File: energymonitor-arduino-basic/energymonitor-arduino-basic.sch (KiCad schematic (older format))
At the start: 12 parts

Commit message: Add conector for 1 wire temperature
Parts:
- added C?: C, symbol Device:C
- added J?: Conn_01x03_Female, symbol Connector:Conn_01x03_Female
- added R?: 4k7, Resistor_THT:R_Axial_DIN0207_L6.3mm_D2.5mm_P10.16mm_Horizontal, symbol Device:R
- J?: value Conn_01x04_Female -> Conn_01x05_Female; symbol Connector:Conn_01x04_Female -> Connector:Conn_01x05_Female
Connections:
- net labels added: 1wire-bus
- wire segments 44 -> 58
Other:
- note added: "9v AC"
- note added: "CT Sensor"
- note added: "DS18B20"
- note added: "Data"
- note added: "Data pull-up resistor"
- note added: "GND"
- note added: "VCC"
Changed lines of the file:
@@
 $EndDescr
 $Comp
-L Connector:Conn_01x04_Female J?
+L Connector:Conn_01x05_Female J?
 U 1 1 62606ACB
-P 7150 1400
-F 0 "J?" H 7178 1376 50  0000 L CNN
-F 1 "Conn_01x04_Female" H 7178 1285 50  0000 L CNN
-F 2 "" H 7150 1400 50  0001 C CNN
-F 3 "~" H 7150 1400 50  0001 C CNN
-	1    7150 1400
-	1    0    0    -1
-$EndComp
-$Comp
-L power:+5V #PWR?
+P 7150 1500
+F 0 "J?" H 7178 1476 50  0000 L CNN
+F 1 "Conn_01x05_Female" H 7178 1385 50  0000 L CNN
+F 2 "" H 7150 1500 50  0001 C CNN
+F 3 "~" H 7150 1500 50  0001 C CNN
+	1    7150 1500
+	1    0    0    -1
+$EndComp
+$Comp
+L power:+5V #PWR0101
 U 1 1 626076B4
 P 6150 1050
-F 0 "#PWR?" H 6150 900 50  0001 C CNN
+F 0 "#PWR0101" H 6150 900 50  0001 C CNN
 F 1 "+5V" H 6165 1223 50  0000 C CNN
 F 2 "" H 6150 1050 50  0001 C CNN
@@
 $EndComp
 $Comp
-L power:GND #PWR?
+L power:GND #PWR0102
 U 1 1 62607C1A
 P 6150 2550
-F 0 "#PWR?" H 6150 2300 50  0001 C CNN
+F 0 "#PWR0102" H 6150 2300 50  0001 C CNN
 F 1 "GND" H 6155 2377 50  0000 C CNN
 F 2 "" H 6150 2550 50  0001 C CNN
@@
 $EndComp
 $Comp
-L power:GND #PWR?
+L power:GND #PWR0103
 U 1 1 6260B66F
 P 2250 2150
-F 0 "#PWR?" H 2250 1900 50  0001 C CNN
+F 0 "#PWR0103" H 2250 1900 50  0001 C CNN
 F 1 "GND" H 2255 1977 50  0000 C CNN
 F 2 "" H 2250 2150 50  0001 C CNN
@@
 NoConn ~ 2450 1500
 $Comp
-L power:GND #PWR?
+L power:GND #PWR0104
 U 1 1 62619158
 P 3350 2800
-F 0 "#PWR?" H 3350 2550 50  0001 C CNN
+F 0 "#PWR0104" H 3350 2550 50  0001 C CNN
 F 1 "GND" H 3355 2627 50  0000 C CNN
 F 2 "" H 3350 2800 50  0001 C CNN
@@
 $EndComp
 $Comp
-L power:+5V #PWR?
+L power:+5V #PWR0105
 U 1 1 62619507
 P 3900 2200
-F 0 "#PWR?" H 3900 2050 50  0001 C CNN
+F 0 "#PWR0105" H 3900 2050 50  0001 C CNN
 F 1 "+5V" V 3915 2328 50  0000 L CNN
 F 2 "" H 3900 2200 50  0001 C CNN
@@
 $EndComp
 $Comp
-L power:+5V #PWR?
+L power:+5V #PWR0106
 U 1 1 6262D570
 P 3900 4300
-F 0 "#PWR?" H 3900 4150 50  0001 C CNN
+F 0 "#PWR0106" H 3900 4150 50  0001 C CNN
 F 1 "+5V" V 3915 4428 50  0000 L CNN
 F 2 "" H 3900 4300 50  0001 C CNN
@@
 $EndComp
 $Comp
-L power:GND #PWR?
+L power:GND #PWR0107
 U 1 1 6262E712
 P 3350 5000
-F 0 "#PWR?" H 3350 4750 50  0001 C CNN
+F 0 "#PWR0107" H 3350 4750 50  0001 C CNN
 F 1 "GND" H 3355 4827 50  0000 C CNN
 F 2 "" H 3350 5000 50  0001 C CNN
@@
 Text Notes 2400 3800 0    50   ~ 0
 Step down voltage divider
+Text Label 6750 1700 2    50   ~ 0
+1wire-bus
+Wire Wire Line
+	6950 1700 6750 1700
+$Comp
+L Connector:Conn_01x03_Female J?
+U 1 1 6261A3BF
+P 5550 3550
+F 0 "J?" H 5442 3225 50  0000 C CNN
+F 1 "Conn_01x03_Female" H 5442 3316 50  0000 C CNN
+F 2 "" H 5550 3550 50  0001 C CNN
+F 3 "~" H 5550 3550 50  0001 C CNN
+	1    5550 3550
+	-1   0    0    1
+$EndComp
+$Comp
+L power:GND #PWR0108
+U 1 1 6261B219
+P 6000 3200
+F 0 "#PWR0108" H 6000 2950 50  0001 C CNN
+F 1 "GND" H 6005 3027 50  0000 C CNN
+F 2 "" H 6000 3200 50  0001 C CNN
+F 3 "" H 6000 3200 50  0001 C CNN
+	1    6000 3200
+	-1   0    0    1
+$EndComp
+$Comp
+L power:+5V #PWR0109
+U 1 1 6261B786
+P 6550 3200
+F 0 "#PWR0109" H 6550 3050 50  0001 C CNN
+F 1 "+5V" H 6565 3373 50  0000 C CNN
+F 2 "" H 6550 3200 50  0001 C CNN
+F 3 "" H 6550 3200 50  0001 C CNN
+	1    6550 3200
+	1    0    0    -1
+$EndComp
+Text Label 7150 3650 0    50   ~ 0
+1wire-bus
+$Comp
+L Device:R R?
+U 1 1 6261CDC5
+P 6800 3550
+F 0 "R?" V 6593 3550 50  0000 C CNN
+F 1 "4k7" V 6684 3550 50  0000 C CNN
+F 2 "Resistor_THT:R_Axial_DIN0207_L6.3mm_D2.5mm_P10.16mm_Horizontal" V 6730 3550 50  0001 C CNN
+F 3 "~" H 6800 3550 50  0001 C CNN
+	1    6800 3550
+	0    1    1    0
+$EndComp
+Wire Wire Line
+	6950 3550 7050 3550
+Wire Wire Line
+	7050 3550 7050 3650
+Connection ~ 7050 3650
+Wire Wire Line
+	7050 3650 7150 3650
+Wire Wire Line
+	6650 3550 6550 3550
+Wire Wire Line
+	6550 3200 6550 3350
+Connection ~ 6550 3550
+Wire Wire Line
+	6000 3200 6000 3350
+Wire Wire Line
+	6000 3450 5750 3450
+Text Notes 7000 3450 0    50   ~ 0
+Data pull-up resistor
+Wire Wire Line
+	5750 3550 6550 3550
+Wire Wire Line
+	5750 3650 7050 3650
+Wire Wire Line
+	6150 3350 6000 3350
+Connection ~ 6000 3350
+Wire Wire Line
+	6000 3350 6000 3450
+Wire Wire Line
+	6450 3350 6550 3350
+Connection ~ 6550 3350
+Wire Wire Line
+	6550 3350 6550 3550
+$Comp
+L Device:C C?
+U 1 1 6263CCEC
+P 6300 3350
+F 0 "C?" V 6048 3350 50  0000 C CNN
+F 1 "C" V 6139 3350 50  0000 C CNN
+F 2 "" H 6338 3200 50  0001 C CNN
+F 3 "~" H 6300 3350 50  0001 C CNN
+	1    6300 3350
+	0    1    1    0
+$EndComp
+Text Notes 5350 3650 0    50   ~ 0
+Data
+Text Notes 5350 3550 0    50   ~ 0
+VCC
+Text Notes 5350 3450 0    50   ~ 0
+GND
+Text Notes 1650 1900 0    50   ~ 0
+CT Sensor
+Text Notes 1750 3850 0    50   ~ 0
+9v AC
+Text Notes 5050 3800 0    50   ~ 0
+DS18B20
 $EndSCHEMATC

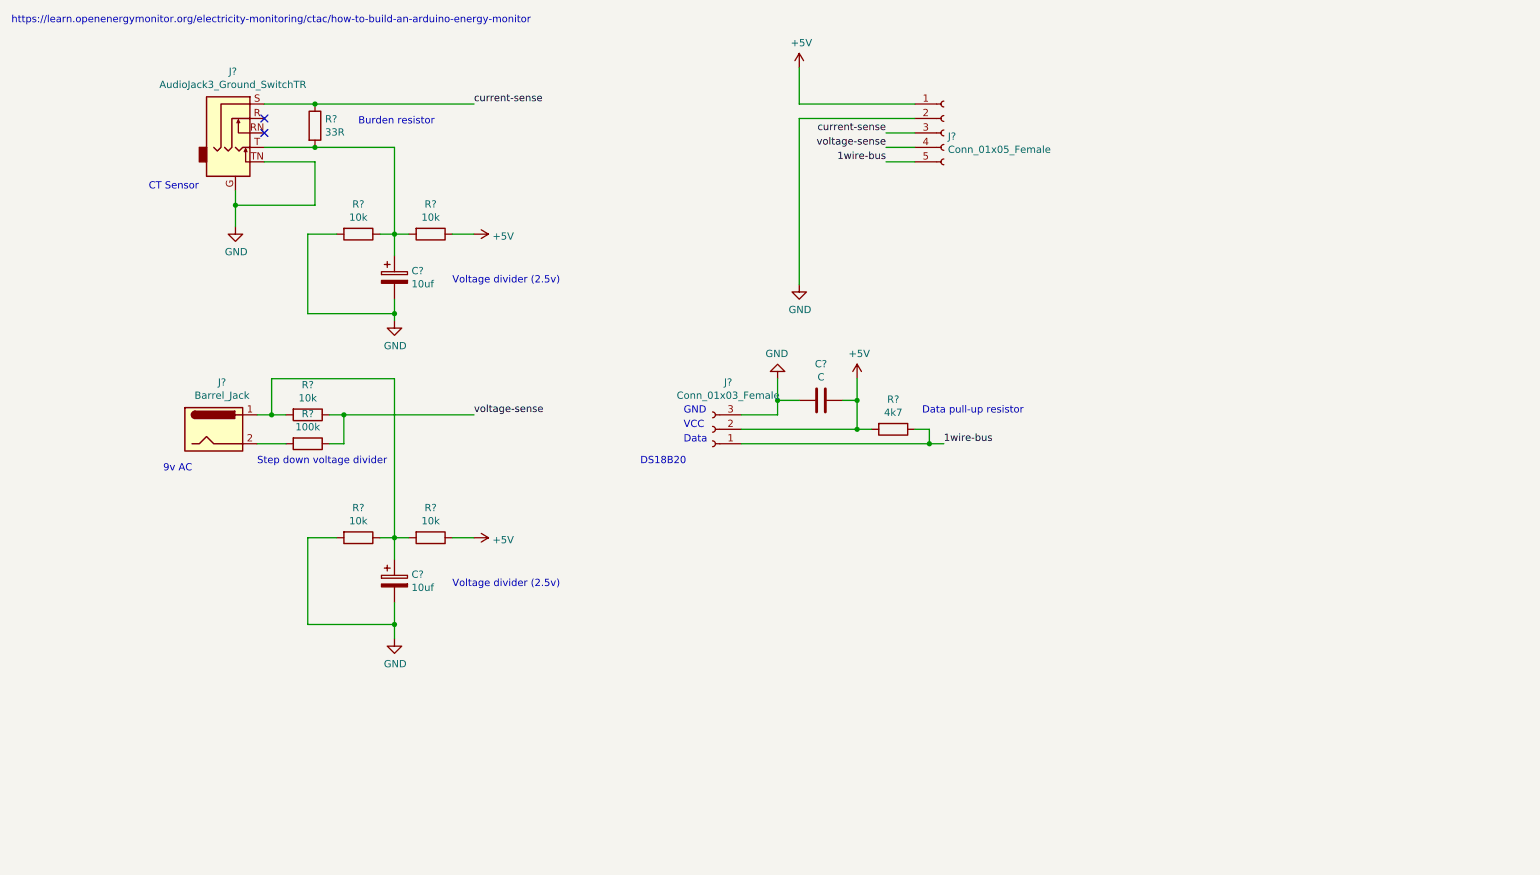
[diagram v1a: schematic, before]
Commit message: Use buffered midpoint voltage
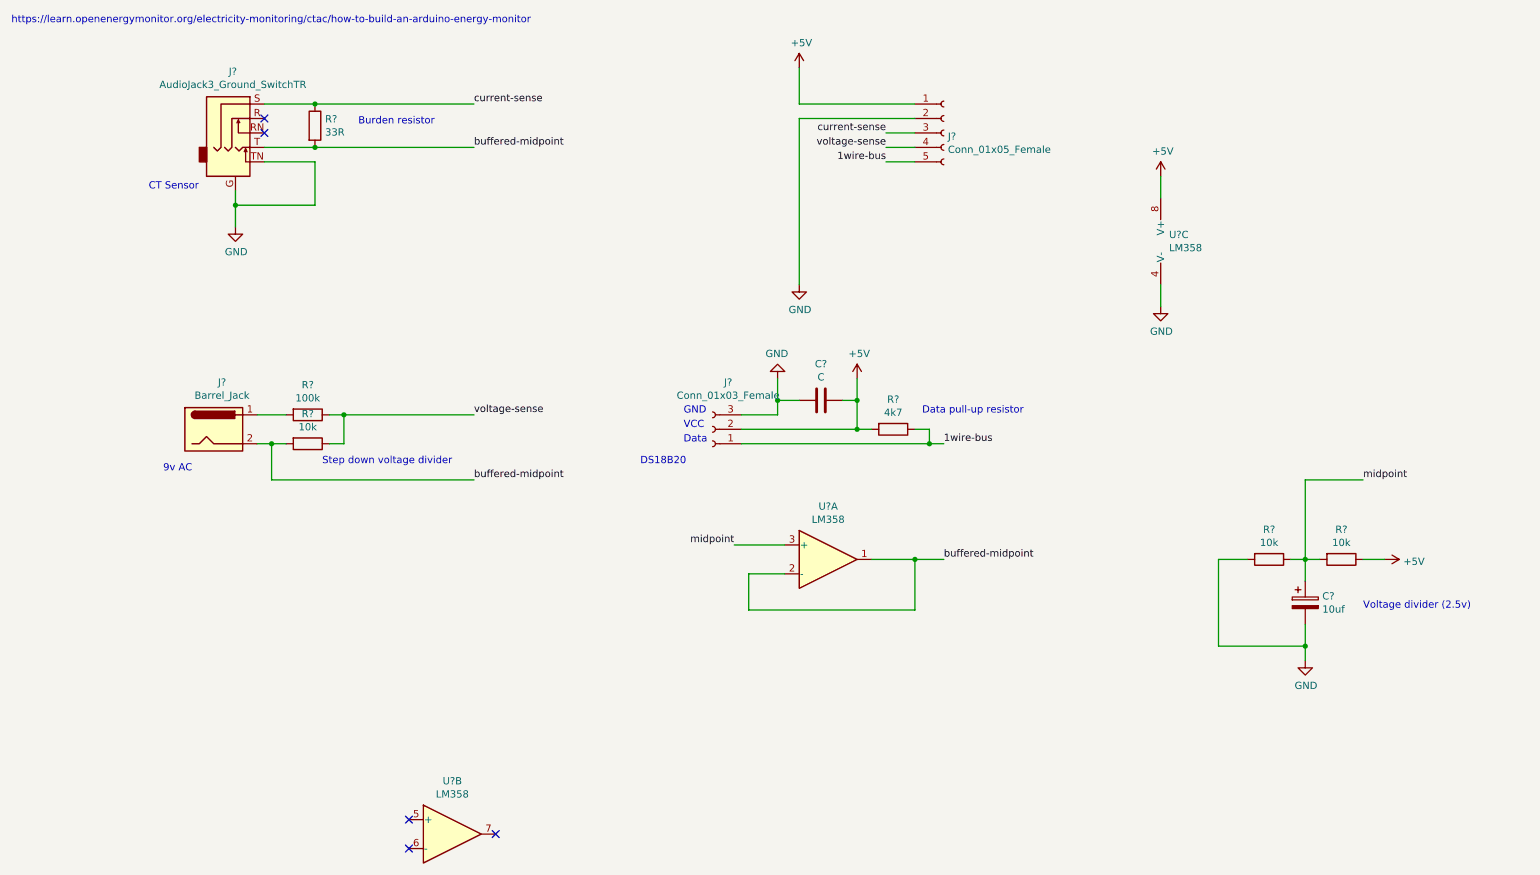
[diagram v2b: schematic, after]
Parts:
- removed C?: 10uf, symbol Device:CP
- removed R? (x2): 10k, Resistor_THT:R_Axial_DIN0207_L6.3mm_D2.5mm_P10.16mm_Horizontal, symbol Device:R
- added U? (x3): LM358, symbol Amplifier_Operational:LM358
- R?: value 10k -> 100k
- R?: value 100k -> 10k
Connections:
- net +5V: now also U?.8 (V+)
- net GND: now also U?.4 (V-)
- net buffered-midpoint: now reaches J?.T, R?.2
- net buffered-midpoint: now also J?.2, R?.2, U?.1, U?.2 (-)
- net midpoint: now reaches C?.1, R?.1, R?.2
- net midpoint: now also U?.3 (+); no longer J?.1, R?.2
- new net: J?.1, R?.2
- no-connect marks 2 -> 5
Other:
- moved on the sheet: C?, R?
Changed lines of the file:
@@
 	2250 2150 2250 2000
-$Comp
-L Device:CP C?
-U 1 1 6260BDA8
-P 3350 2500
-F 0 "C?" H 3468 2546 50  0000 L CNN
-F 1 "10uf" H 3468 2455 50  0000 L CNN
-F 2 "" H 3388 2350 50  0001 C CNN
-F 3 "~" H 3350 2500 50  0001 C CNN
-	1    3350 2500
-	1    0    0    -1
-$EndComp
-$Comp
-L Device:R R?
-U 1 1 6260C4FE
-P 3100 2200
-F 0 "R?" V 2893 2200 50  0000 C CNN
-F 1 "10k" V 2984 2200 50  0000 C CNN
-F 2 "Resistor_THT:R_Axial_DIN0207_L6.3mm_D2.5mm_P10.16mm_Horizontal" V 3030 2200 50  0001 C CNN
-F 3 "~" H 3100 2200 50  0001 C CNN
-	1    3100 2200
-	0    1    1    0
-$EndComp
-$Comp
-L Device:R R?
-U 1 1 6260C5C9
-P 3600 2200
-F 0 "R?" V 3393 2200 50  0000 C CNN
-F 1 "10k" V 3484 2200 50  0000 C CNN
-F 2 "Resistor_THT:R_Axial_DIN0207_L6.3mm_D2.5mm_P10.16mm_Horizontal" V 3530 2200 50  0001 C CNN
-F 3 "~" H 3600 2200 50  0001 C CNN
-	1    3600 2200
-	0    1    1    0
-$EndComp
 $Comp
 L Device:R R?
@@
 NoConn ~ 2450 1400
 NoConn ~ 2450 1500
-$Comp
-L power:GND #PWR0104
-U 1 1 62619158
-P 3350 2800
-F 0 "#PWR0104" H 3350 2550 50  0001 C CNN
-F 1 "GND" H 3355 2627 50  0000 C CNN
-F 2 "" H 3350 2800 50  0001 C CNN
-F 3 "" H 3350 2800 50  0001 C CNN
-	1    3350 2800
-	1    0    0    -1
-$EndComp
-$Comp
-L power:+5V #PWR0105
-U 1 1 62619507
-P 3900 2200
-F 0 "#PWR0105" H 3900 2050 50  0001 C CNN
-F 1 "+5V" V 3915 2328 50  0000 L CNN
-F 2 "" H 3900 2200 50  0001 C CNN
-F 3 "" H 3900 2200 50  0001 C CNN
-	1    3900 2200
-	0    1    1    0
-$EndComp
-Wire Wire Line
-	3250 2200 3350 2200
-Wire Wire Line
-	3350 2350 3350 2200
-Connection ~ 3350 2200
-Wire Wire Line
-	3350 2200 3450 2200
-Wire Wire Line
-	3900 2200 3750 2200
-Wire Wire Line
-	2950 2200 2750 2200
-Wire Wire Line
-	2750 2200 2750 2750
-Wire Wire Line
-	2750 2750 3350 2750
-Wire Wire Line
-	3350 2750 3350 2650
-Wire Wire Line
-	3350 2800 3350 2750
-Connection ~ 3350 2750
-Wire Wire Line
-	3350 2200 3350 1600
-Wire Wire Line
-	3350 1600 2800 1600
 Connection ~ 2800 1600
 Text Label 3900 1300 0    50   ~ 0
@@
 L Device:R R?
 U 1 1 6262BC5E
-P 3100 4300
-F 0 "R?" V 2893 4300 50  0000 C CNN
-F 1 "10k" V 2984 4300 50  0000 C CNN
-F 2 "Resistor_THT:R_Axial_DIN0207_L6.3mm_D2.5mm_P10.16mm_Horizontal" V 3030 4300 50  0001 C CNN
-F 3 "~" H 3100 4300 50  0001 C CNN
-	1    3100 4300
+P 9400 4450
+F 0 "R?" V 9193 4450 50  0000 C CNN
+F 1 "10k" V 9284 4450 50  0000 C CNN
+F 2 "Resistor_THT:R_Axial_DIN0207_L6.3mm_D2.5mm_P10.16mm_Horizontal" V 9330 4450 50  0001 C CNN
+F 3 "~" H 9400 4450 50  0001 C CNN
+	1    9400 4450
 	0    1    1    0
 $EndComp
@@
 L Device:R R?
 U 1 1 6262C6E4
-P 3600 4300
-F 0 "R?" V 3393 4300 50  0000 C CNN
-F 1 "10k" V 3484 4300 50  0000 C CNN
-F 2 "Resistor_THT:R_Axial_DIN0207_L6.3mm_D2.5mm_P10.16mm_Horizontal" V 3530 4300 50  0001 C CNN
-F 3 "~" H 3600 4300 50  0001 C CNN
-	1    3600 4300
+P 9900 4450
+F 0 "R?" V 9693 4450 50  0000 C CNN
+F 1 "10k" V 9784 4450 50  0000 C CNN
+F 2 "Resistor_THT:R_Axial_DIN0207_L6.3mm_D2.5mm_P10.16mm_Horizontal" V 9830 4450 50  0001 C CNN
+F 3 "~" H 9900 4450 50  0001 C CNN
+	1    9900 4450
 	0    1    1    0
 $EndComp
@@
 L Device:CP C?
 U 1 1 6262CCE6
-P 3350 4600
-F 0 "C?" H 3468 4646 50  0000 L CNN
-F 1 "10uf" H 3468 4555 50  0000 L CNN
-F 2 "" H 3388 4450 50  0001 C CNN
-F 3 "~" H 3350 4600 50  0001 C CNN
-	1    3350 4600
+P 9650 4750
+F 0 "C?" H 9768 4796 50  0000 L CNN
+F 1 "10uf" H 9768 4705 50  0000 L CNN
+F 2 "" H 9688 4600 50  0001 C CNN
+F 3 "~" H 9650 4750 50  0001 C CNN
+	1    9650 4750
 	1    0    0    -1
 $EndComp
@@
 L power:+5V #PWR0106
 U 1 1 6262D570
-P 3900 4300
-F 0 "#PWR0106" H 3900 4150 50  0001 C CNN
-F 1 "+5V" V 3915 4428 50  0000 L CNN
-F 2 "" H 3900 4300 50  0001 C CNN
-F 3 "" H 3900 4300 50  0001 C CNN
-	1    3900 4300
+P 10200 4450
+F 0 "#PWR0106" H 10200 4300 50  0001 C CNN
+F 1 "+5V" V 10215 4578 50  0000 L CNN
+F 2 "" H 10200 4450 50  0001 C CNN
+F 3 "" H 10200 4450 50  0001 C CNN
+	1    10200 4450
 	0    1    1    0
 $EndComp
@@
 L power:GND #PWR0107
 U 1 1 6262E712
-P 3350 5000
-F 0 "#PWR0107" H 3350 4750 50  0001 C CNN
-F 1 "GND" H 3355 4827 50  0000 C CNN
-F 2 "" H 3350 5000 50  0001 C CNN
-F 3 "" H 3350 5000 50  0001 C CNN
-	1    3350 5000
-	1    0    0    -1
-$EndComp
-Wire Wire Line
-	3750 4300 3900 4300
-Wire Wire Line
-	3450 4300 3350 4300
-Wire Wire Line
-	3350 4450 3350 4300
-Connection ~ 3350 4300
-Wire Wire Line
-	3350 4300 3250 4300
-Wire Wire Line
-	2950 4300 2750 4300
-Wire Wire Line
-	2750 4300 2750 4900
-Wire Wire Line
-	2750 4900 3350 4900
-Wire Wire Line
-	3350 4900 3350 5000
-Wire Wire Line
-	3350 4900 3350 4750
-Connection ~ 3350 4900
+P 9650 5150
+F 0 "#PWR0107" H 9650 4900 50  0001 C CNN
+F 1 "GND" H 9655 4977 50  0000 C CNN
+F 2 "" H 9650 5150 50  0001 C CNN
+F 3 "" H 9650 5150 50  0001 C CNN
+	1    9650 5150
+	1    0    0    -1
+$EndComp
+Wire Wire Line
+	10050 4450 10200 4450
+Wire Wire Line
+	9750 4450 9650 4450
+Wire Wire Line
+	9650 4600 9650 4450
+Connection ~ 9650 4450
+Wire Wire Line
+	9650 4450 9550 4450
+Wire Wire Line
+	9250 4450 9050 4450
+Wire Wire Line
+	9050 4450 9050 5050
+Wire Wire Line
+	9050 5050 9650 5050
+Wire Wire Line
+	9650 5050 9650 5150
+Wire Wire Line
+	9650 5050 9650 4900
+Connection ~ 9650 5050
 Text Label 3900 3450 0    50   ~ 0
 voltage-sense
@@
 P 2750 3450
 F 0 "R?" V 2543 3450 50  0000 C CNN
-F 1 "10k" V 2634 3450 50  0000 C CNN
+F 1 "100k" V 2634 3450 50  0000 C CNN
 F 2 "Resistor_THT:R_Axial_DIN0207_L6.3mm_D2.5mm_P10.16mm_Horizontal" V 2680 3450 50  0001 C CNN
 F 3 "~" H 2750 3450 50  0001 C CNN
@@
 P 2750 3650
 F 0 "R?" V 2543 3650 50  0000 C CNN
-F 1 "100k" V 2634 3650 50  0000 C CNN
+F 1 "10k" V 2634 3650 50  0000 C CNN
 F 2 "Resistor_THT:R_Axial_DIN0207_L6.3mm_D2.5mm_P10.16mm_Horizontal" V 2680 3650 50  0001 C CNN
 F 3 "~" H 2750 3650 50  0001 C CNN
@@
 $EndComp
 Wire Wire Line
-	2400 3450 2500 3450
-Wire Wire Line
-	3350 4300 3350 3200
-Wire Wire Line
-	3350 3200 2500 3200
-Wire Wire Line
-	2500 3200 2500 3450
-Connection ~ 2500 3450
-Wire Wire Line
-	2500 3450 2600 3450
-Wire Wire Line
 	2900 3450 3000 3450
 Wire Wire Line
@@
 	3000 3450 3900 3450
 Wire Wire Line
-	2400 3650 2600 3650
+	2400 3650 2500 3650
 Text Notes 700  750  0    50   ~ 0
 https://learn.openenergymonitor.org/electricity-monitoring/ctac/how-to-build-an-arduino-energy-monitor
-Text Notes 3750 4650 0    50   ~ 0
-Voltage divider (2.5v)
-Text Notes 3750 2550 0    50   ~ 0
+Text Notes 10050 4800 0    50   ~ 0
 Voltage divider (2.5v)
 Text Notes 3100 1450 0    50   ~ 0
 Burden resistor
-Text Notes 2400 3800 0    50   ~ 0
+Text Notes 2850 3800 0    50   ~ 0
 Step down voltage divider
 Text Label 6750 1700 2    50   ~ 0
@@
 Text Notes 5050 3800 0    50   ~ 0
 DS18B20
+$Comp
+L Amplifier_Operational:LM358 U?
+U 1 1 6278D4CE
+P 6350 4450
+F 0 "U?" H 6350 4817 50  0000 C CNN
+F 1 "LM358" H 6350 4726 50  0000 C CNN
+F 2 "" H 6350 4450 50  0001 C CNN
+F 3 "http://www.ti.com/lit/ds/symlink/lm2904-n.pdf" H 6350 4450 50  0001 C CNN
+	1    6350 4450
+	1    0    0    -1
+$EndComp
+$Comp
+L Amplifier_Operational:LM358 U?
+U 2 1 6278EB53
+P 3750 6350
+F 0 "U?" H 3750 6717 50  0000 C CNN
+F 1 "LM358" H 3750 6626 50  0000 C CNN
+F 2 "" H 3750 6350 50  0001 C CNN
+F 3 "http://www.ti.com/lit/ds/symlink/lm2904-n.pdf" H 3750 6350 50  0001 C CNN
+	2    3750 6350
+	1    0    0    -1
+$EndComp
+$Comp
+L Amplifier_Operational:LM358 U?
+U 3 1 6278FD5E
+P 8750 2250
+F 0 "U?" H 8708 2296 50  0000 L CNN
+F 1 "LM358" H 8708 2205 50  0000 L CNN
+F 2 "" H 8750 2250 50  0001 C CNN
+F 3 "http://www.ti.com/lit/ds/symlink/lm2904-n.pdf" H 8750 2250 50  0001 C CNN
+	3    8750 2250
+	1    0    0    -1
+$EndComp
+Wire Wire Line
+	6650 4450 6950 4450
+Wire Wire Line
+	6950 4450 6950 4800
+Wire Wire Line
+	6950 4800 5800 4800
+Wire Wire Line
+	5800 4800 5800 4550
+Wire Wire Line
+	5800 4550 6050 4550
+$Comp
+L power:GND #PWR?
+U 1 1 627A363E
+P 8650 2700
+F 0 "#PWR?" H 8650 2450 50  0001 C CNN
+F 1 "GND" H 8655 2527 50  0000 C CNN
+F 2 "" H 8650 2700 50  0001 C CNN
+F 3 "" H 8650 2700 50  0001 C CNN
+	1    8650 2700
+	1    0    0    -1
+$EndComp
+$Comp
+L power:+5V #PWR?
+U 1 1 627A3F4D
+P 8650 1800
+F 0 "#PWR?" H 8650 1650 50  0001 C CNN
+F 1 "+5V" H 8665 1973 50  0000 C CNN
+F 2 "" H 8650 1800 50  0001 C CNN
+F 3 "" H 8650 1800 50  0001 C CNN
+	1    8650 1800
+	1    0    0    -1
+$EndComp
+Wire Wire Line
+	8650 1800 8650 1950
+Wire Wire Line
+	8650 2550 8650 2700
+NoConn ~ 3450 6250
+NoConn ~ 3450 6450
+NoConn ~ 4050 6350
+Text Label 7150 4450 0    50   ~ 0
+buffered-midpoint
+Text Label 5700 4350 2    50   ~ 0
+midpoint
+Wire Wire Line
+	5700 4350 6050 4350
+Wire Wire Line
+	7150 4450 6950 4450
+Connection ~ 6950 4450
+Text Label 10050 3900 0    50   ~ 0
+midpoint
+Wire Wire Line
+	10050 3900 9650 3900
+Wire Wire Line
+	9650 3900 9650 4450
+Text Label 3900 3900 0    50   ~ 0
+buffered-midpoint
+Text Label 3900 1600 0    50   ~ 0
+buffered-midpoint
+Wire Wire Line
+	2800 1600 3900 1600
+Wire Wire Line
+	2500 3900 3900 3900
+Wire Wire Line
+	2400 3450 2600 3450
+Wire Wire Line
+	2500 3900 2500 3650
+Connection ~ 2500 3650
+Wire Wire Line
+	2500 3650 2600 3650
 $EndSCHEMATC
